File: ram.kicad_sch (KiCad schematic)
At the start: 7 parts, among them U10 HyperRAM

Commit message: kicad: fix LED PD, APMem, 1V8, USB ~RST short
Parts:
- U10: value HyperRAM -> PSRAM (oSPI /HyperRAM); Manufacturer Winbond -> (none); Part Number W956A8MBYA6I -> (none); Substitution W956A8MBYA5I -> (none); lcsc# C7428856 -> C5448342
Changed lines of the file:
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@@
 			)
 		)
-		(property "Value" "HyperRAM"
+		(property "Value" "PSRAM (oSPI /HyperRAM)"
 			(at 137.16 81.7372 0)
 			(effects
@@
 			)
 		)
-		(property "Description" "DRAM 64Mb HyperRAM x8, 166MHz, Ind temp, 3.0V"
+		(property "Description" ""
 			(at 137.16 102.87 0)
 			(effects
@@
 			)
 		)
-		(property "Manufacturer" "Winbond"
+		(property "Manufacturer" ""
 			(at 137.16 102.87 0)
 			(effects
@@
 			)
 		)
-		(property "Part Number" "W956A8MBYA6I"
+		(property "Part Number" ""
 			(at 137.16 102.87 0)
 			(effects
@@
 			)
 		)
-		(property "Substitution" "W956A8MBYA5I"
+		(property "Substitution" ""
 			(at 137.16 102.87 0)
 			(effects
@@
 			)
 		)
-		(property "lcsc#" "C7428856 "
+		(property "lcsc#" "C5448342"
 			(at 137.16 102.87 0)
 			(effects

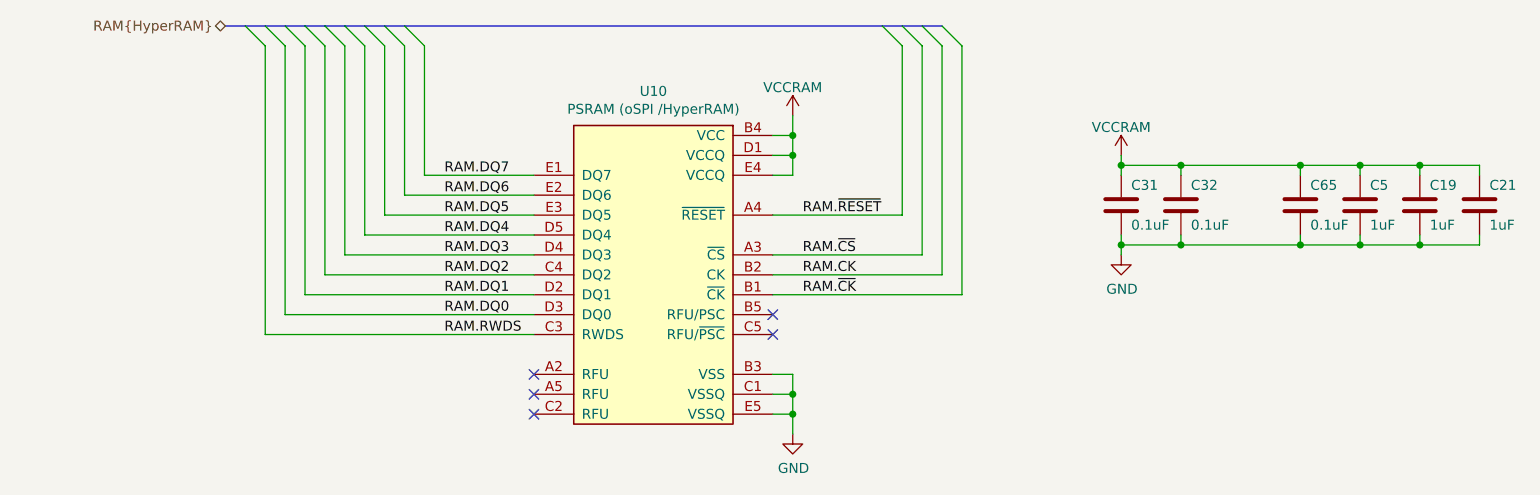
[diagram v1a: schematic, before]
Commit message: sch: capture 16-bit bus
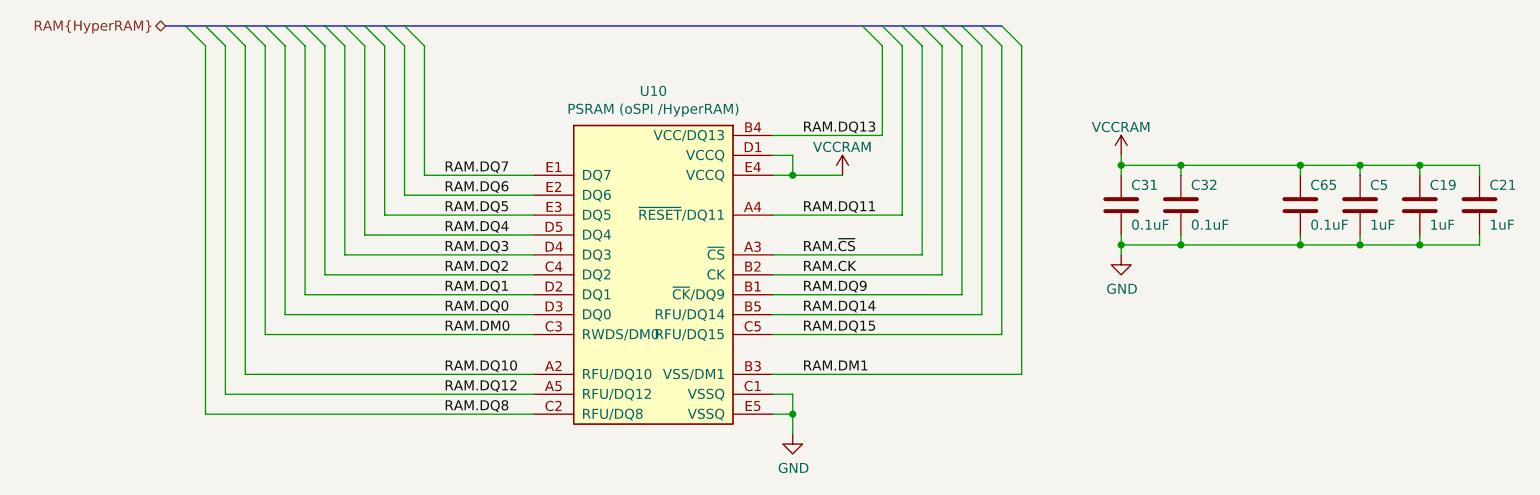
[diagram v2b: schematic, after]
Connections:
- net GND: no longer U10.B3 (VSS)
- net VCCRAM: no longer U10.B4 (VCC)
- net RAM.DQ10: now reaches U10.A2 (RFU/DQ10)
- net RAM.DQ12: now reaches U10.A5 (RFU/DQ12)
- net RAM.DQ14: now reaches U10.B5 (RFU/DQ14)
- net RAM.DQ8: now reaches U10.C2 (RFU/DQ8)
- net RAM.DQ15: now reaches U10.C5 (RFU/DQ15)
- net RAM.RWDS renamed RAM.DM0
- net RAM.~{CK} renamed RAM.DQ9
- net RAM.~{RESET} renamed RAM.DQ11
- new net RAM.DM1: U10.B3 (VSS/DM1)
- new net RAM.DQ13: U10.B4 (VCC/DQ13)
- no-connect marks 5 -> 0
